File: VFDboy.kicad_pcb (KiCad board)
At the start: 2 copper layers, 139.5 x 60 mm, 108 parts, among them J1 AVR-ISP-6, J2 USB_C_Receptacle_USB2.0, J3 Micro_SD_Card_Det, J4 TagConnect_TC2030_SWD, Q1 FS8205A, Q2 S9015, Q3 AO3401A, Q4 AO3401A, Q5 S9015, Q6 2N7002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

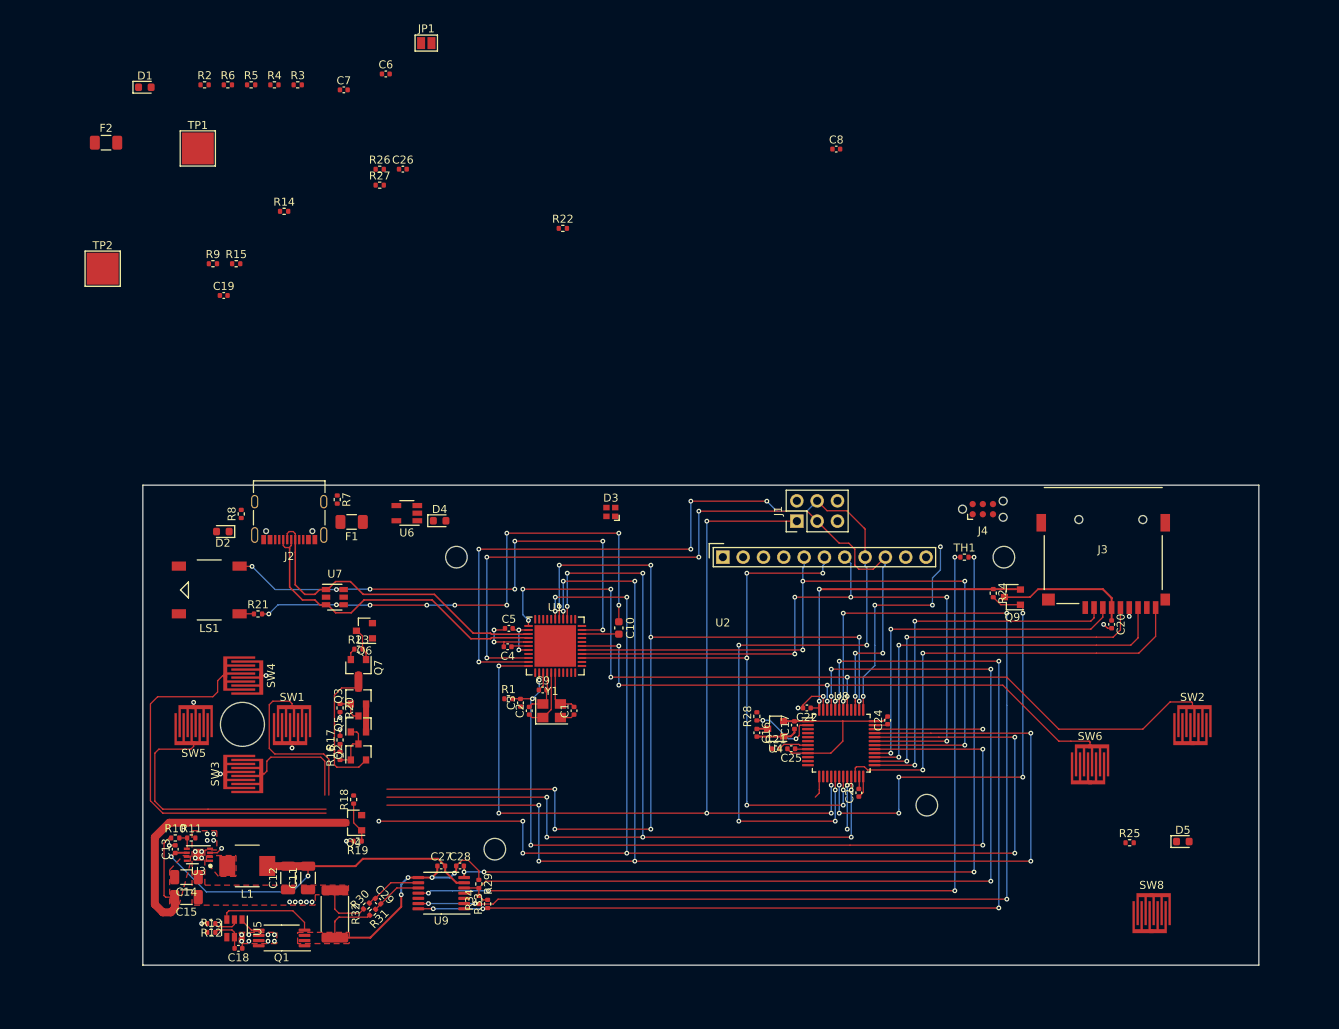
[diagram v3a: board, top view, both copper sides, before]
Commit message: route VFD power
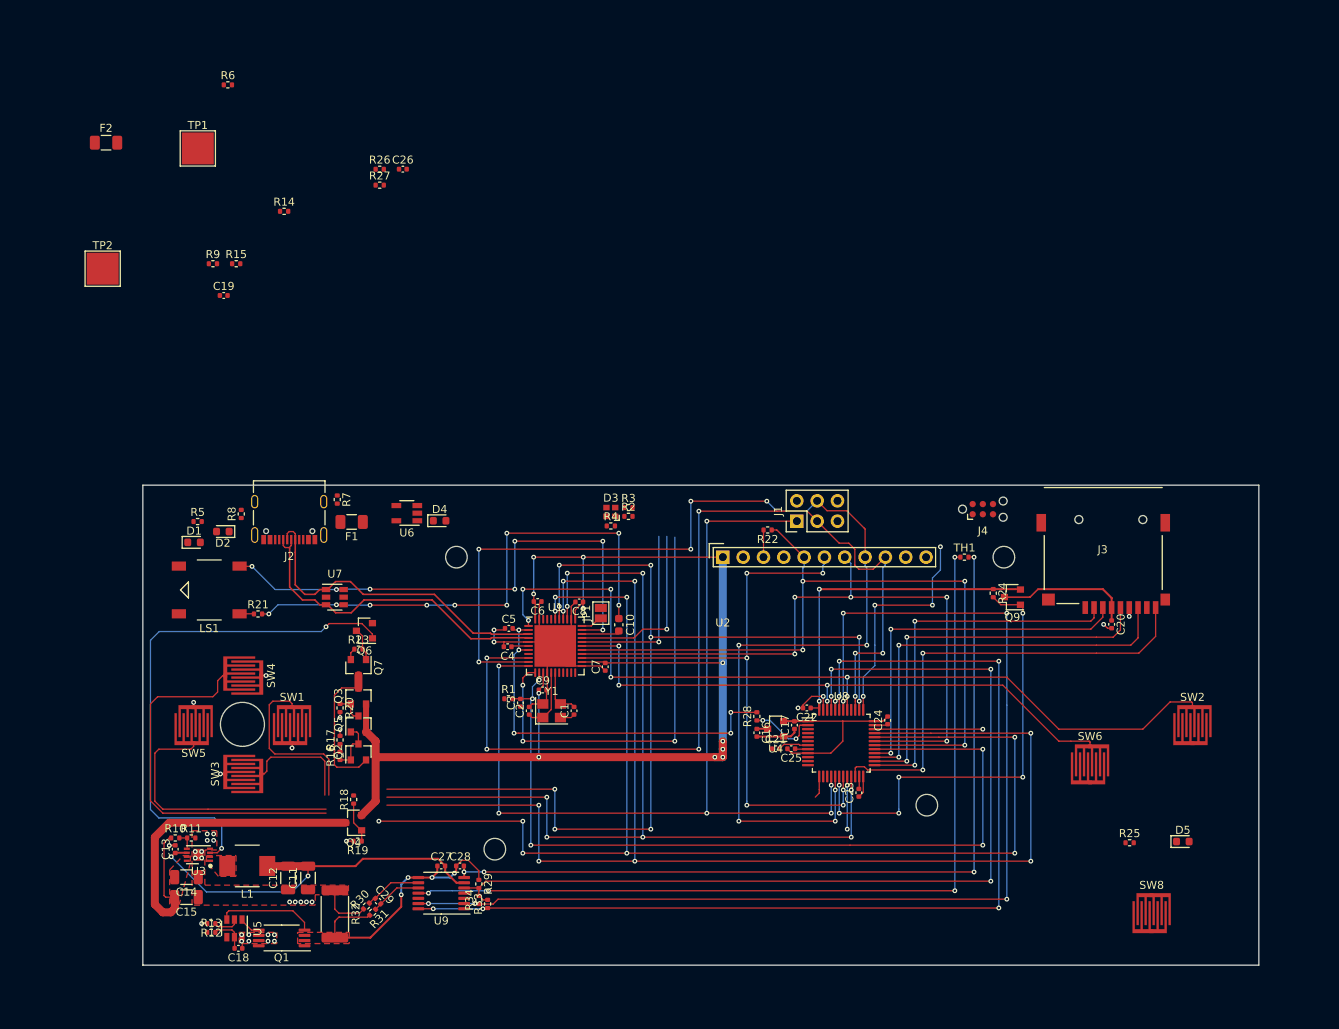
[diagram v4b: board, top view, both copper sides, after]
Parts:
- moved C7 79.2 mm to (160.3, 122.7), turned to 90 degrees
- moved R2 75.6 mm to (163.2, 103.9)
- moved JP1 74.5 mm to (159.8, 116.0), turned to 90 degrees
- moved R4 69.3 mm to (161.0, 105.1)
- moved C6 68.6 mm to (151.8, 114.5), turned to 180 degrees
- moved R3 67.1 mm to (163.2, 102.8)
- moved C8 65.1 mm to (157.1, 114.6), turned to 180 degrees
- moved D1 57.2 mm to (108.9, 107.2)
- moved R5 55.0 mm to (109.3, 104.5)
- moved R22 45.6 mm to (180.6, 105.6), turned to 180 degrees
- moved C10 0.40 mm to (162.0, 117.5)
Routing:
- net +5V: track 5.89 -> 156.2 mm, vias 0 -> 11
- net /Power/PWR_EN: track 1.68 -> 65.1 mm, vias 1 -> 2
- net Net-(R4-Pad2): track 0.00 -> 54.2 mm, vias 0 -> 3
- net VBUS: track 7.25 -> 50.8 mm, vias 2 -> 5
- net Net-(R2-Pad2): track 0.00 -> 22.8 mm, vias 0 -> 1
- net /SCK: track 100.9 -> 123.7 mm
- net Net-(R3-Pad2): track 0.00 -> 22.7 mm, vias 0 -> 1
- net GND: track 47.2 -> 66.1 mm
- net /~OLEDRST: track 91.3 -> 96.8 mm
- net Net-(JP1-Pad1): track 0.00 -> 2.83 mm

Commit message: Finish layout
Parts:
- added C30: 100nF, Capacitor_SMD:C_0402_1005Metric, F.Cu at (187.2, 138.8)
- added C31: 47uF, Capacitor_SMD:C_1206_3216Metric, F.Cu at (175.0, 114.8)
- added Q8: 2N7002, Package_TO_SOT_SMD:SOT-23, F.Cu at (142.3, 103.8)
- added R35: 1MR, Resistor_SMD:R_0402_1005Metric, F.Cu at (131.8, 121.0)
- added R36: 8.2kR, Resistor_SMD:R_0402_1005Metric, F.Cu at (135.7, 102.2)
- C19: value 1uF -> 10uF; footprint Capacitor_SMD:C_0402_1005Metric -> Capacitor_SMD:C_0603_1608Metric
- C26: value 100nF -> 10uF; footprint Capacitor_SMD:C_0402_1005Metric -> Capacitor_SMD:C_0603_1608Metric
- D1, D2, D5: footprint Diode_SMD:D_0603_1608Metric -> LED_SMD:LED_0603_1608Metric
- R26: value 8.2kR -> 2.2kR
- TP1, TP2: moved to B.Cu
- U6: value TP4054 -> TP4056; footprint Package_TO_SOT_SMD:TSOT-23-5 -> Package_SO:HSOP-8-1EP_3.9x4.9mm_P1.27mm_EP2.41x3.1mm
- moved F2 91.6 mm to (122.0, 145.5)
- moved TP1 87.9 mm to (124.8, 144.4)
- moved R6 87.6 mm to (156.6, 126.1), turned to 90 degrees
- moved TP2 86.2 mm to (118.7, 156.5)
- moved R9 71.9 mm to (114.3, 144.2)
- moved C26 49.2 mm to (130.8, 109.5), turned to 90 degrees
- moved R26 44.1 mm to (139.3, 104.0)
- moved R25 41.3 mm to (185.3, 136.9), turned to 90 degrees
- moved R5 39.3 mm to (145.3, 120.5)
- moved R27 38.9 mm to (133.8, 101.3), turned to 270 degrees
- moved R14 38.0 mm to (132.0, 101.8), turned to 180 degrees
- moved R15 37.8 mm to (135.7, 103.5)
- moved C19 33.8 mm to (133.1, 103.2), turned to 180 degrees
- moved D4 10.6 mm to (129.3, 101.8)
- moved D1 5.80 mm to (114.5, 105.7), turned to 90 degrees
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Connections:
- net Net-(Q6-Pad3) renamed /Power/~PWR_EN
- C26 pad 1: GND -> +BATT
- C26 pad 2: /Power/Ichg -> GND
- D1 pad 2: Net-(D1-Pad2) -> +5V
- D2 pad 2: Net-(D2-Pad2) -> +5V
- R26 pad 2: /Power/Ichg -> Net-(Q8-Pad3)
- R5 pad 1: +5V -> Net-(D1-Pad1)
- R5 pad 2: Net-(D1-Pad2) -> Net-(R5-Pad2)
- R6 pad 1: +5V -> Net-(D2-Pad1)
- R6 pad 2: Net-(D2-Pad2) -> Net-(R6-Pad2)
- U1 pad 22: Net-(D2-Pad1) -> Net-(R6-Pad2)
- U1 pad 8: Net-(D1-Pad1) -> Net-(R5-Pad2)
- U6 pad 1: /Power/LEDchg -> GND
- U6 pad 2: GND -> Net-(R15-Pad1)
- U6 pad 3: +BATT -> GND
- U6 pad 5: Net-(R15-Pad1) -> +BATT
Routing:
- net +BATT: track 51.2 -> 222.6 mm, vias 2 -> 16
- net /Power/LEDchg: track 6.59 -> 126.3 mm, vias 2 -> 6
- net /STM32/~STMRST: track 3.81 -> 112.9 mm, vias 0 -> 4
- net /Power/PWR_EN: track 65.1 -> 152.7 mm, vias 2 -> 6
- net /Power/Ichg: track 2.79 -> 90.3 mm, vias 0 -> 2
- net Net-(SW8-Pad1): track 0.00 -> 80.8 mm, vias 0 -> 4
- net +5V: track 156.2 -> 233.6 mm, vias 11 -> 22
- net Net-(D2-Pad1): track 0.00 -> 76.2 mm, vias 0 -> 4
- net Net-(D5-Pad2): track 0.00 -> 72.2 mm, vias 0 -> 4
- net +3V3: track 67.8 -> 139.8 mm, vias 2 -> 4
- net VBUS: track 50.8 -> 115.6 mm, vias 5 -> 16
- net Net-(D1-Pad1): track 0.00 -> 44.7 mm
- net /~RST: track 106.5 -> 146.6 mm, vias 5 -> 8
- net GND: track 66.1 -> 103.7 mm, vias 29 -> 60
- net Net-(J4-Pad2): track 13.5 -> 48.2 mm, vias 1 -> 2
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- added copper zone on B.Cu, net GND
- added copper zone on F.Cu, net Net-(F1-Pad2)

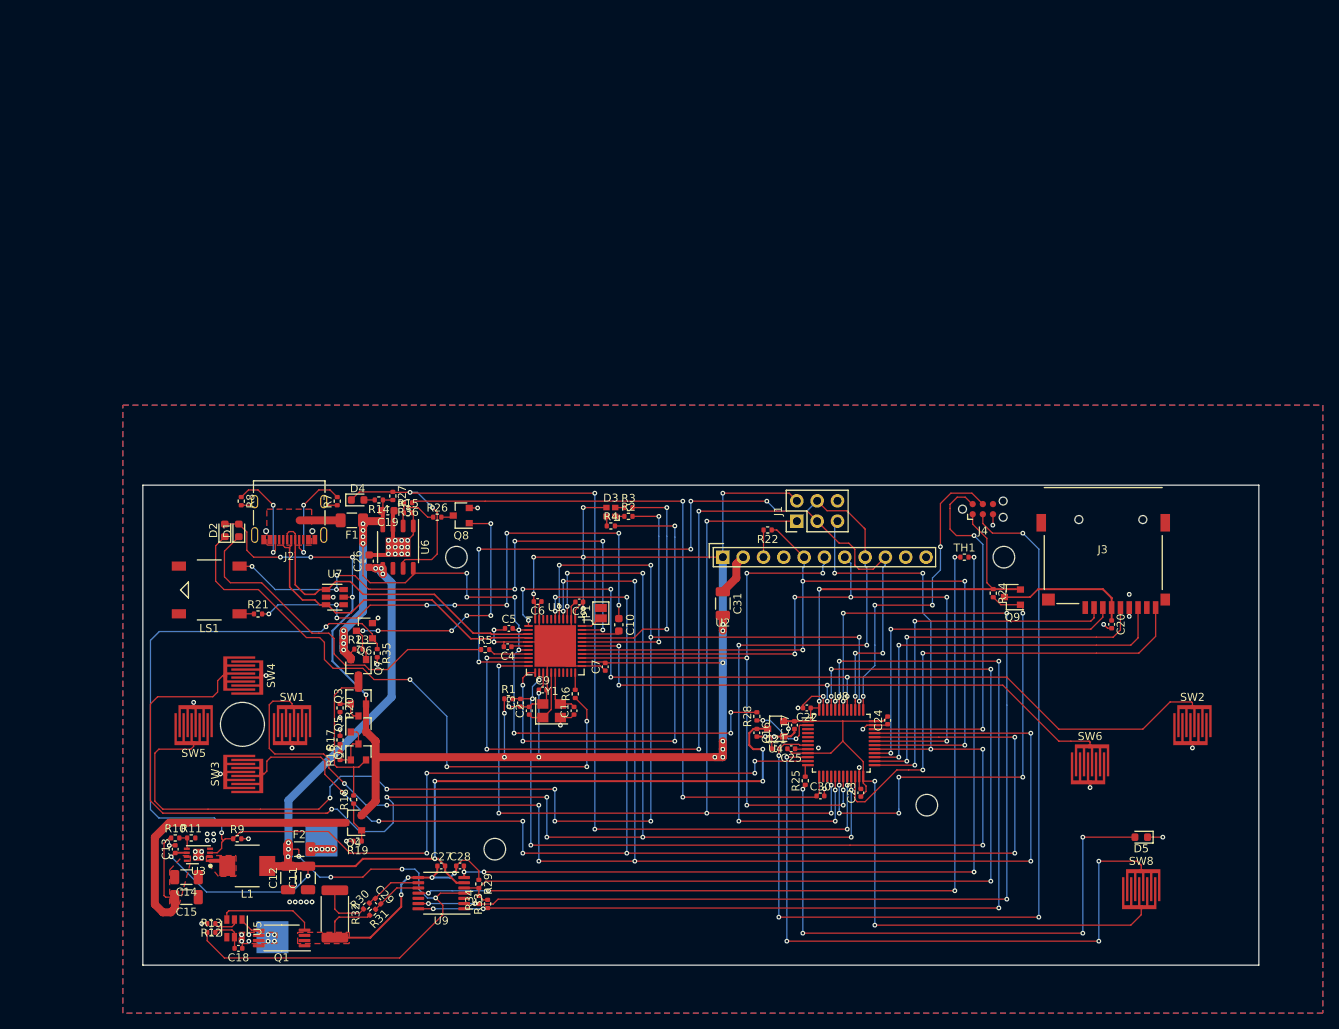
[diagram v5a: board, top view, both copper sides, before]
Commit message: Add additional mounting holes
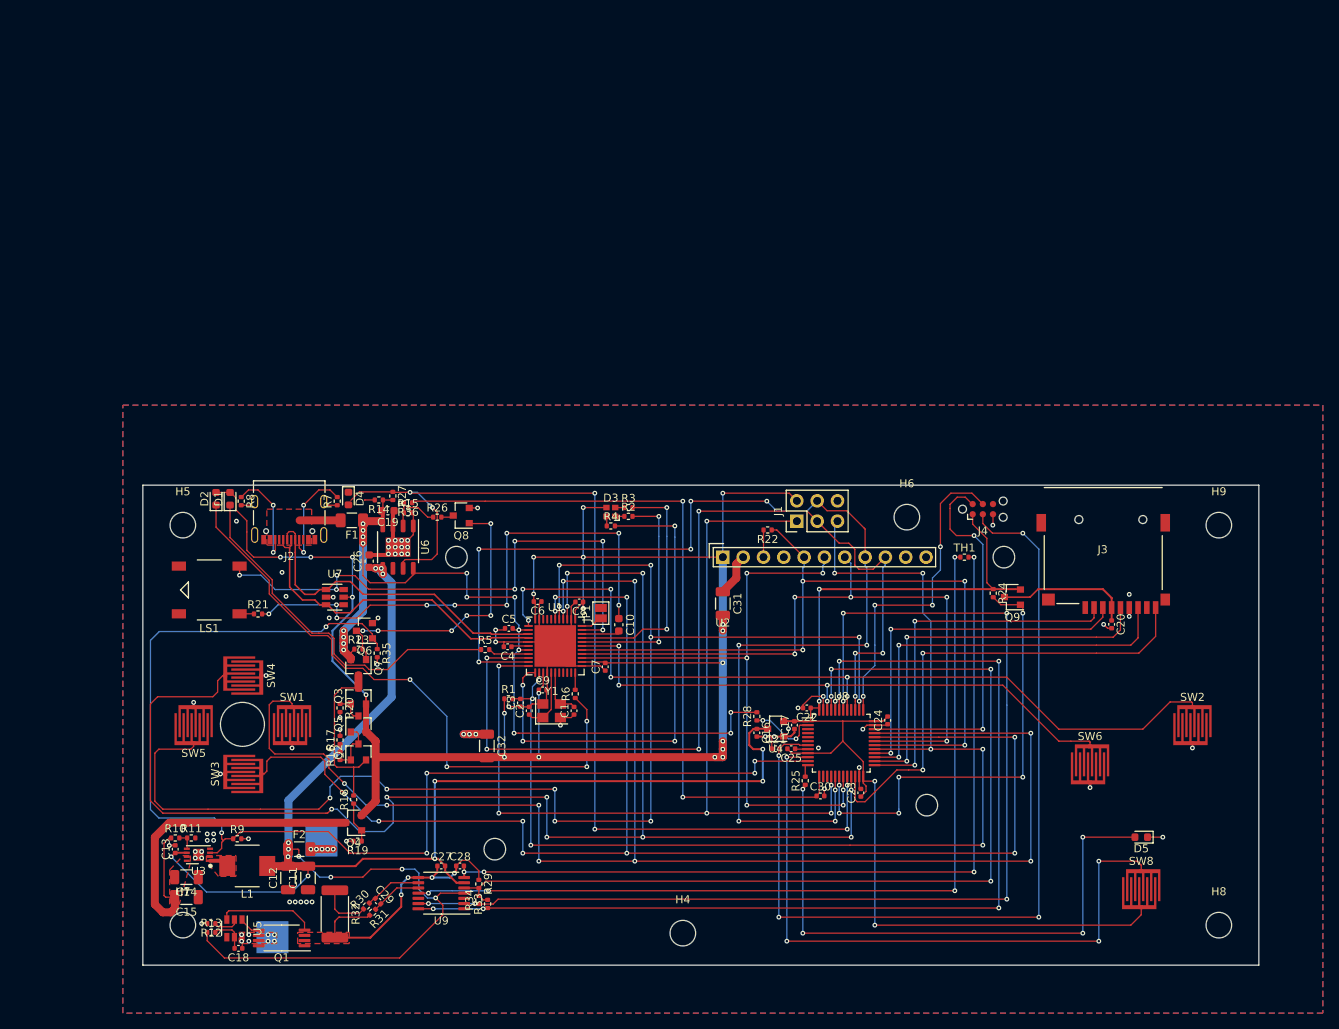
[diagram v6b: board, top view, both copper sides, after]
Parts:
- added C32: 47uF, Capacitor_SMD:C_1206_3216Metric, F.Cu at (145.5, 132.6)
- added H4: MountingHole, MountingHole:MountingHole_3.2mm_M3, F.Cu at (170.0, 156.0)
- added H5: MountingHole, MountingHole:MountingHole_3.2mm_M3, F.Cu at (107.5, 105.0)
- added H6: MountingHole, MountingHole:MountingHole_3.2mm_M3, F.Cu at (198.0, 104.0)
- added H7: MountingHole, MountingHole:MountingHole_3.2mm_M3, F.Cu at (107.5, 155.0)
- added H8: MountingHole, MountingHole:MountingHole_3.2mm_M3, F.Cu at (237.0, 155.0)
- added H9: MountingHole, MountingHole:MountingHole_3.2mm_M3, F.Cu at (237.0, 105.0)
- moved D1 4.10 mm to (113.4, 101.7)
- moved D2 4.10 mm to (111.7, 101.7)
- moved D4 1.16 mm to (128.2, 101.7), turned to 270 degrees
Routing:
- net GND: track 103.7 -> 108.1 mm, vias 60 -> 67
- net +5V: track 233.6 -> 237.9 mm
- net Net-(D1-Pad1): track 44.7 -> 45.5 mm
- net /SPKR-: track 69.7 -> 70.4 mm

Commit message: Add VFD 3D model
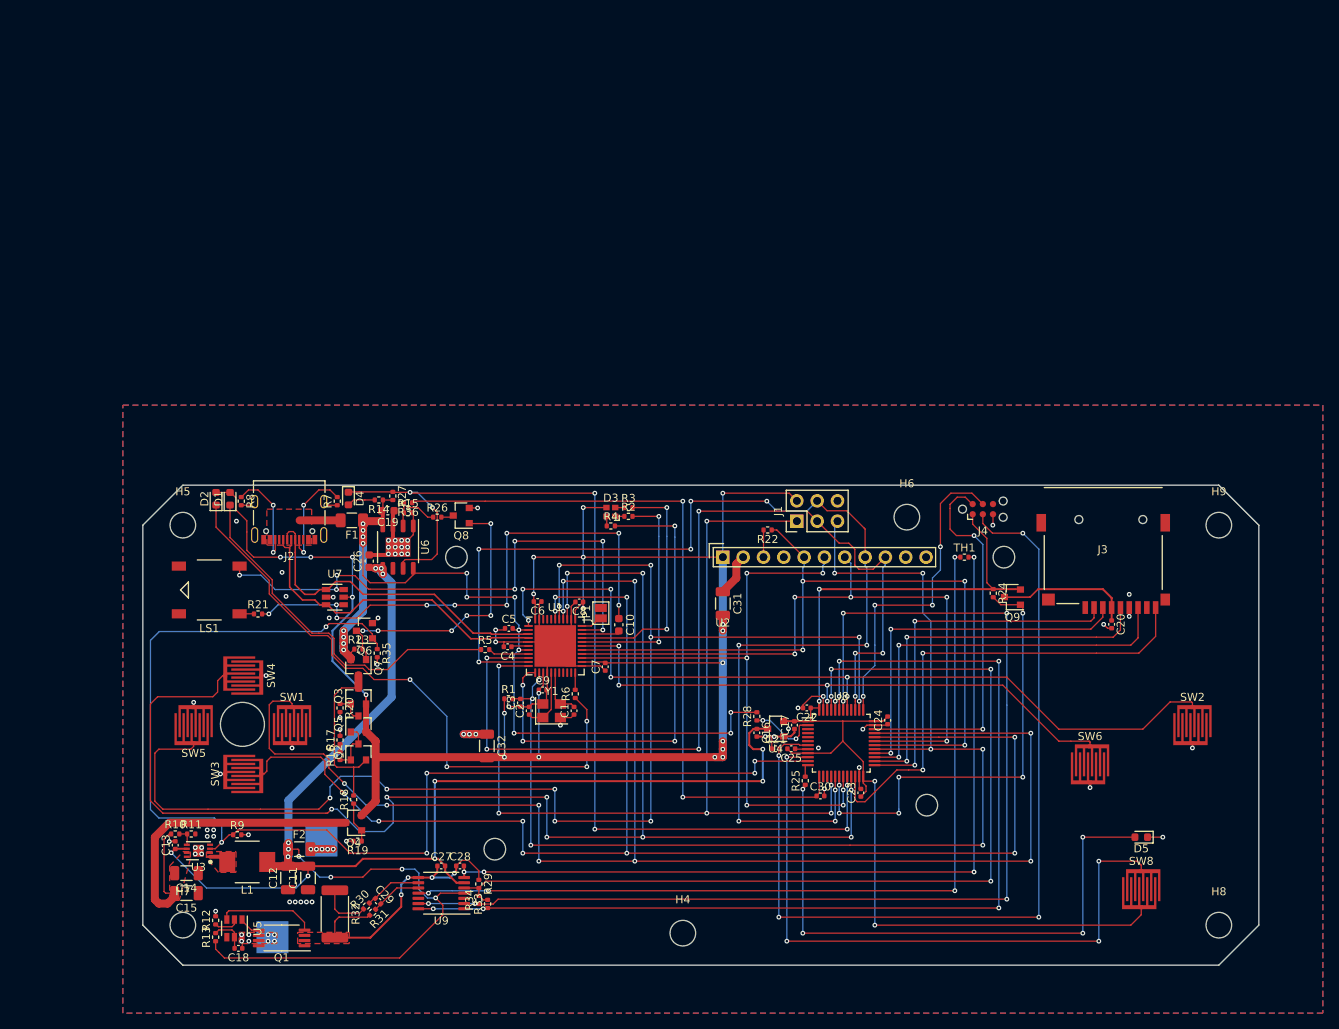
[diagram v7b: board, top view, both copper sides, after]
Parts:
- moved R13 0.81 mm to (111.6, 156.5), turned to 90 degrees
- moved R12 0.68 mm to (111.6, 154.4), turned to 90 degrees
- moved C13 0.50 mm to (106.5, 145.0)
- moved C14 0.50 mm to (108.0, 148.5)
- moved C15 0.50 mm to (108.0, 151.0)
- moved L1 0.50 mm to (115.5, 147.1)
- moved R10 0.50 mm to (106.5, 143.6)
- moved R11 0.50 mm to (108.5, 143.6)
- moved R9 0.50 mm to (114.3, 143.7)
- moved U3 0.50 mm to (109.5, 145.7)
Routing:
- net Net-(D4-Pad2): track 1.31 -> 3.56 mm
- net /Power/Power switch/VSTEP_UP: track 46.4 -> 44.3 mm
- net +BATT: track 222.6 -> 220.8 mm
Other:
- outline, holes or cut-outs redrawn

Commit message: Add last 3d models
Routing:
- net +BATT: track 220.8 -> 220.2 mm
- net /Power/PWR_EN: track 152.4 -> 151.8 mm
- net GND: vias 67 -> 371
